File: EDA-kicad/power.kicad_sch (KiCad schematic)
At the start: 93 parts, among them SW1 EG25-switch-CSS-1210MC, SW2 MIC-switch-CSS-1210MC, SW3 CAM-switch-CSS-1210MC, U10 22V-boost-AP3032KTR-G1, U11 MP3429GL-Z, U7 BQ25792RQMR, U8 TPS65023BRSBR, U9 BAT-CONNECTOR-FLTS22WR00

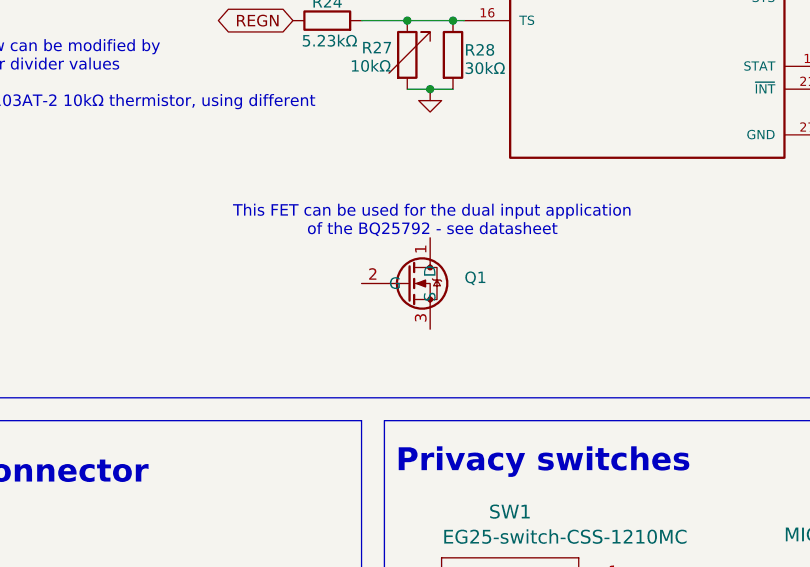
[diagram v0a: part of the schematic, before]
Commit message: added polarity detection
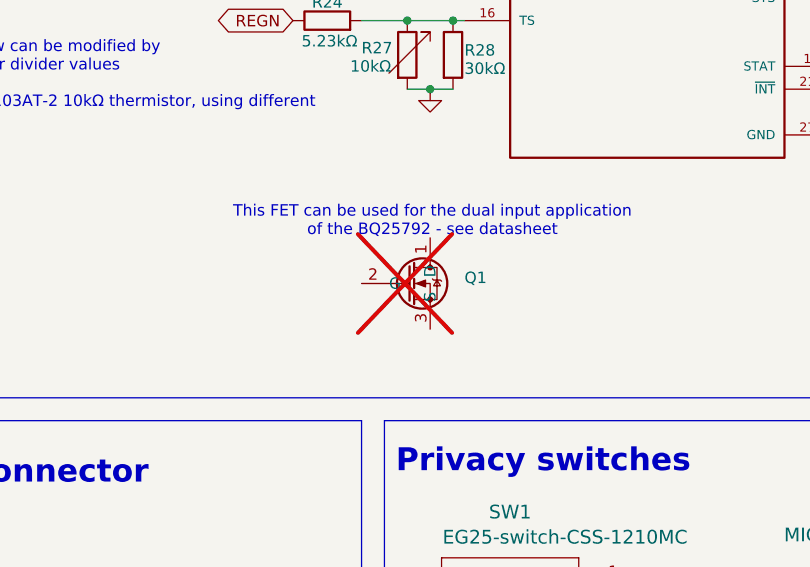
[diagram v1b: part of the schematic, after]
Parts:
- Q1: now not fitted
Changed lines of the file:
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@@
 		)
 		(instances
-			(project ""
+			(project "cm5-carrier"
 				(path "/28c5e4fe-1ec7-4477-97f0-d2ec1401fad5/59851108-1ec5-49a1-aa9b-d5428f895885"
 					(reference "TP5")
@@
 		)
 		(instances
-			(project ""
+			(project "cm5-carrier"
 				(path "/28c5e4fe-1ec7-4477-97f0-d2ec1401fad5/59851108-1ec5-49a1-aa9b-d5428f895885"
 					(reference "L6")
@@
 		)
 		(instances
-			(project ""
+			(project "cm5-carrier"
 				(path "/28c5e4fe-1ec7-4477-97f0-d2ec1401fad5/59851108-1ec5-49a1-aa9b-d5428f895885"
 					(reference "SW1")
@@
 		)
 		(instances
-			(project ""
+			(project "cm5-carrier"
 				(path "/28c5e4fe-1ec7-4477-97f0-d2ec1401fad5/59851108-1ec5-49a1-aa9b-d5428f895885"
 					(reference "R11")
@@
 		)
 		(instances
-			(project ""
+			(project "cm5-carrier"
 				(path "/28c5e4fe-1ec7-4477-97f0-d2ec1401fad5/59851108-1ec5-49a1-aa9b-d5428f895885"
 					(reference "U10")
@@
 		)
 		(instances
-			(project ""
+			(project "cm5-carrier"
 				(path "/28c5e4fe-1ec7-4477-97f0-d2ec1401fad5/59851108-1ec5-49a1-aa9b-d5428f895885"
 					(reference "L5")
@@
 		)
 		(instances
-			(project ""
+			(project "cm5-carrier"
 				(path "/28c5e4fe-1ec7-4477-97f0-d2ec1401fad5/59851108-1ec5-49a1-aa9b-d5428f895885"
 					(reference "R13")
@@
 		)
 		(instances
-			(project ""
+			(project "cm5-carrier"
 				(path "/28c5e4fe-1ec7-4477-97f0-d2ec1401fad5/59851108-1ec5-49a1-aa9b-d5428f895885"
 					(reference "L3")
@@
 		)
 		(instances
-			(project ""
+			(project "cm5-carrier"
 				(path "/28c5e4fe-1ec7-4477-97f0-d2ec1401fad5/59851108-1ec5-49a1-aa9b-d5428f895885"
 					(reference "D1")
@@
 		)
 		(instances
-			(project ""
+			(project "cm5-carrier"
 				(path "/28c5e4fe-1ec7-4477-97f0-d2ec1401fad5/59851108-1ec5-49a1-aa9b-d5428f895885"
 					(reference "F1")
@@
 		(in_bom yes)
 		(on_board yes)
-		(dnp no)
+		(dnp yes)
 		(fields_autoplaced yes)
 		(property "Reference" "Q1"
@@
 		)
 		(instances
-			(project ""
+			(project "cm5-carrier"
 				(path "/28c5e4fe-1ec7-4477-97f0-d2ec1401fad5/59851108-1ec5-49a1-aa9b-d5428f895885"
 					(reference "Q1")
@@
 		)
 		(instances
-			(project ""
+			(project "cm5-carrier"
 				(path "/28c5e4fe-1ec7-4477-97f0-d2ec1401fad5/59851108-1ec5-49a1-aa9b-d5428f895885"
 					(reference "U8")
@@
 		)
 		(instances
-			(project ""
+			(project "cm5-carrier"
 				(path "/28c5e4fe-1ec7-4477-97f0-d2ec1401fad5/59851108-1ec5-49a1-aa9b-d5428f895885"
 					(reference "R29")
@@
 		)
 		(instances
-			(project ""
+			(project "cm5-carrier"
 				(path "/28c5e4fe-1ec7-4477-97f0-d2ec1401fad5/59851108-1ec5-49a1-aa9b-d5428f895885"
 					(reference "U11")
